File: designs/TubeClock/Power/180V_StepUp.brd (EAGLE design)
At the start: 52 x 39 mm, 16 parts, among them IC1 MAX1771, Q1 RF644

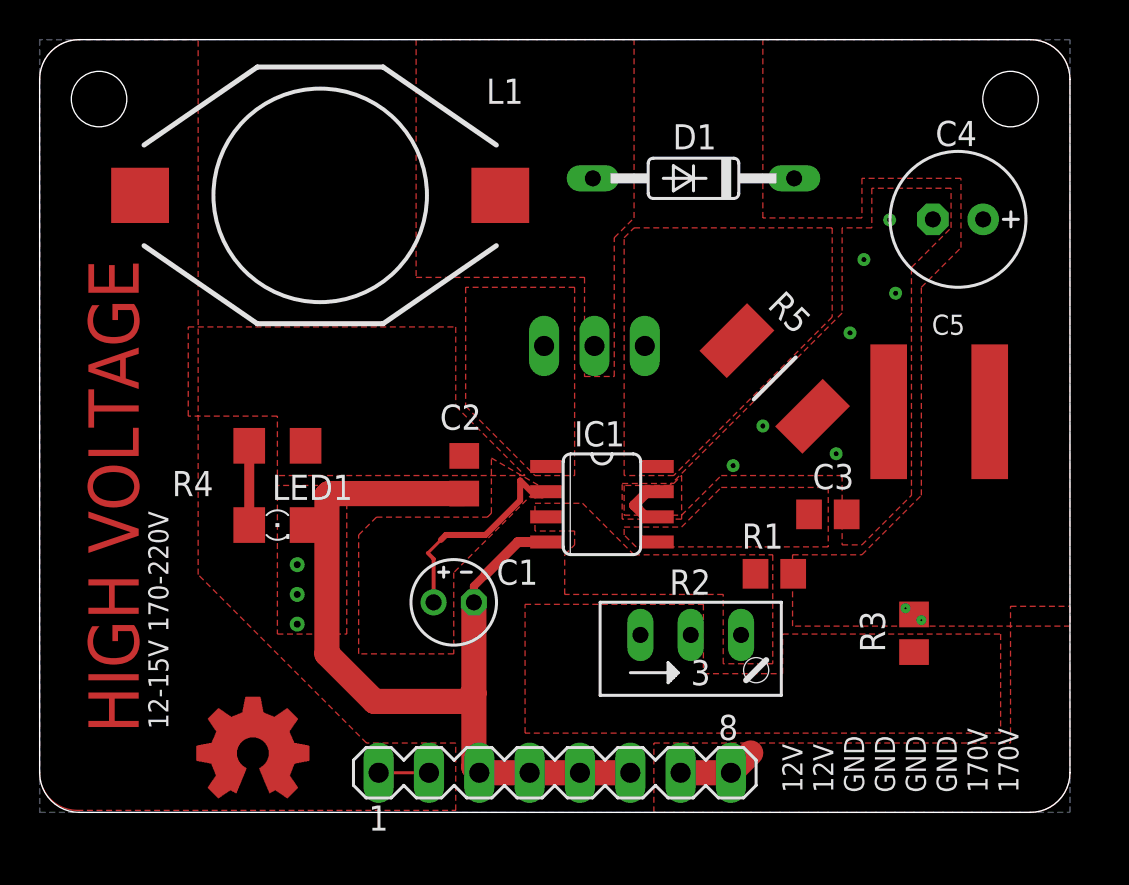
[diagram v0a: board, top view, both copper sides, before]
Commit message: small changes to easter radio mainboard started for in14 nixi tubes and cleanup
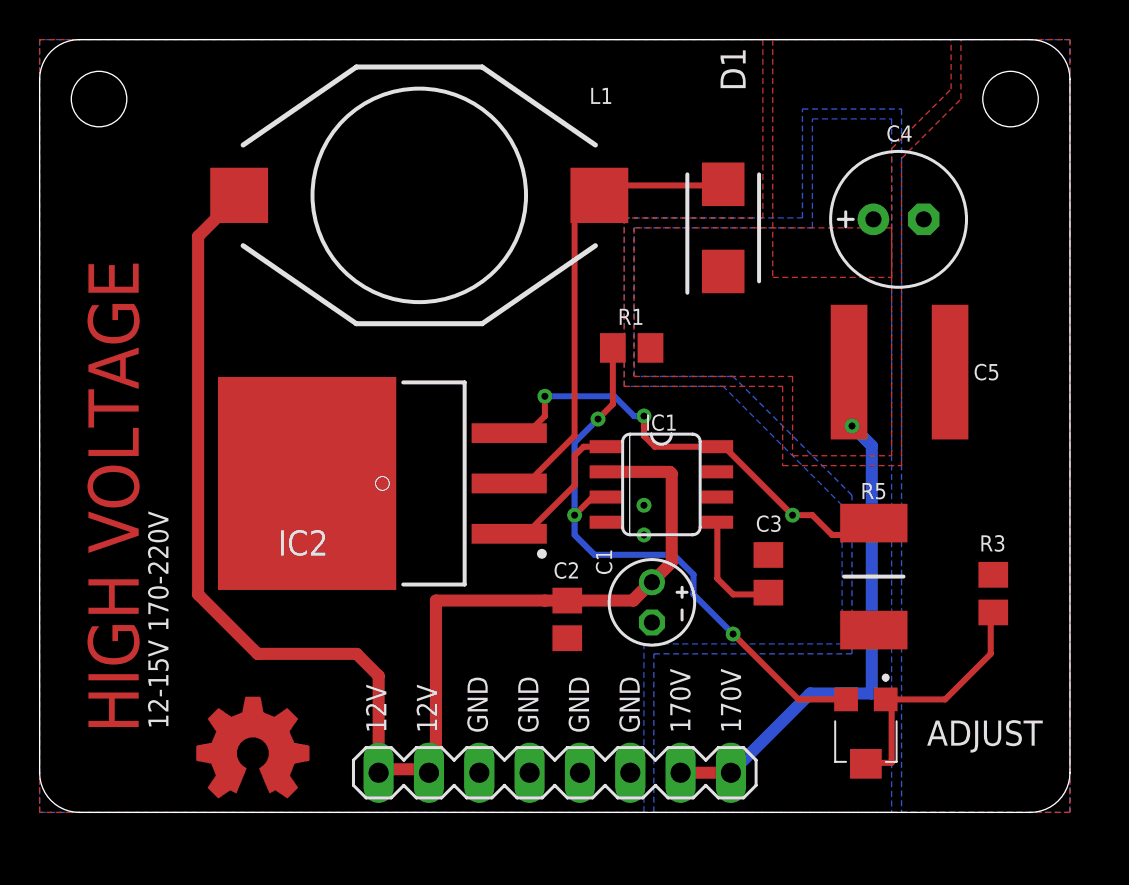
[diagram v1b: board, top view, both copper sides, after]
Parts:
- removed LED1: GREEN, CommonParts:1206
- removed Q1: RF644, transistor-power:TO220BV
- removed R2: 10k, pot:RJ9W
- removed R4: 1K, CommonParts:R1206
- removed SV2: (no value), con-lstb:MA08-1
- added ADJUST: EVM3YSX50B14, CommonParts:EVM3YSX50B14
- added IC2: IRF644SPBF, MouserUseful:TO254P1524X483-4N
- added SV1: (no value), CommonParts:MA08-1
- D1: value 1N4148DO35-10 -> LSM115JE3_TR13; device diode:DO35-10 -> CommonParts:DIOM5436X330N
- moved R1 13.5 mm to (28.9, 23.4)
- moved R5 11.2 mm to (41.1, 11.9), turned to 90 degrees
- moved C1 10.0 mm to (29.9, 10.6), turned to 270 degrees
- moved C2 8.96 mm to (25.6, 9.74)
- moved L1 5.00 mm to (18.2, 31.1)
- moved R3 4.47 mm to (47.1, 11.0)
- moved C3 4.24 mm to (35.8, 12.0), turned to 90 degrees
- moved IC1 3.16 mm to (30.4, 16.6)
- moved C4 3.00 mm to (42.4, 29.9), turned to 0 degrees
- moved D1 2.92 mm to (33.5, 29.5), turned to 90 degrees
- moved C5 2.83 mm to (42.4, 22.2), turned to 0 degrees
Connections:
- removed net N$1: LED1.A, R4.2
- net +170V: now also D1.1, SV1.7, SV1.8; no longer D1.C, SV2.7, SV2.8
- net GND: now also SV1.3, SV1.4, SV1.5, SV1.6; no longer LED1.C, SV2.3, SV2.4, SV2.5, SV2.6
- net N$2: now also D1.2, IC2.2; no longer D1.A, Q1.D
- net N$4: now also IC2.1; no longer Q1.G
- net N$5: now also IC2.3; no longer Q1.S
- net N$6: now also ADJUST.C1; no longer R2.A
- net N$7: now also ADJUST.A1, ADJUST.B1; no longer R2.E, R2.S
- net VIN: now also SV1.1, SV1.2; no longer R4.1, SV2.1, SV2.2
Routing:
- net VIN: track 14.4 -> 75.0 mm
- net GND: track 48.8 -> 0.00 mm, vias 12 -> 2
- net N$6: track 0.00 -> 29.9 mm, vias 0 -> 3
- net N$2: track 0.00 -> 23.8 mm
- net N$5: track 0.00 -> 23.8 mm, vias 0 -> 3
- net +170V: track 3.95 -> 25.2 mm, vias 0 -> 1
- net N$7: track 0.00 -> 12.9 mm
- net N$4: track 0.00 -> 7.56 mm
- net N$3: track 0.00 -> 5.79 mm
- net N$1: track 4.00 -> 0.00 mm
- added copper zone on layer 16, net +170V
- removed copper zone on layer 1, net N$2
- removed copper zone on layer 1, net N$3
- removed copper zone on layer 1, net N$4
- removed copper zone on layer 1, net N$5
- removed copper zone on layer 1, net N$6
- removed copper zone on layer 1, net N$7
- removed copper zone on layer 1, net VIN

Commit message: changed mainboard design radio
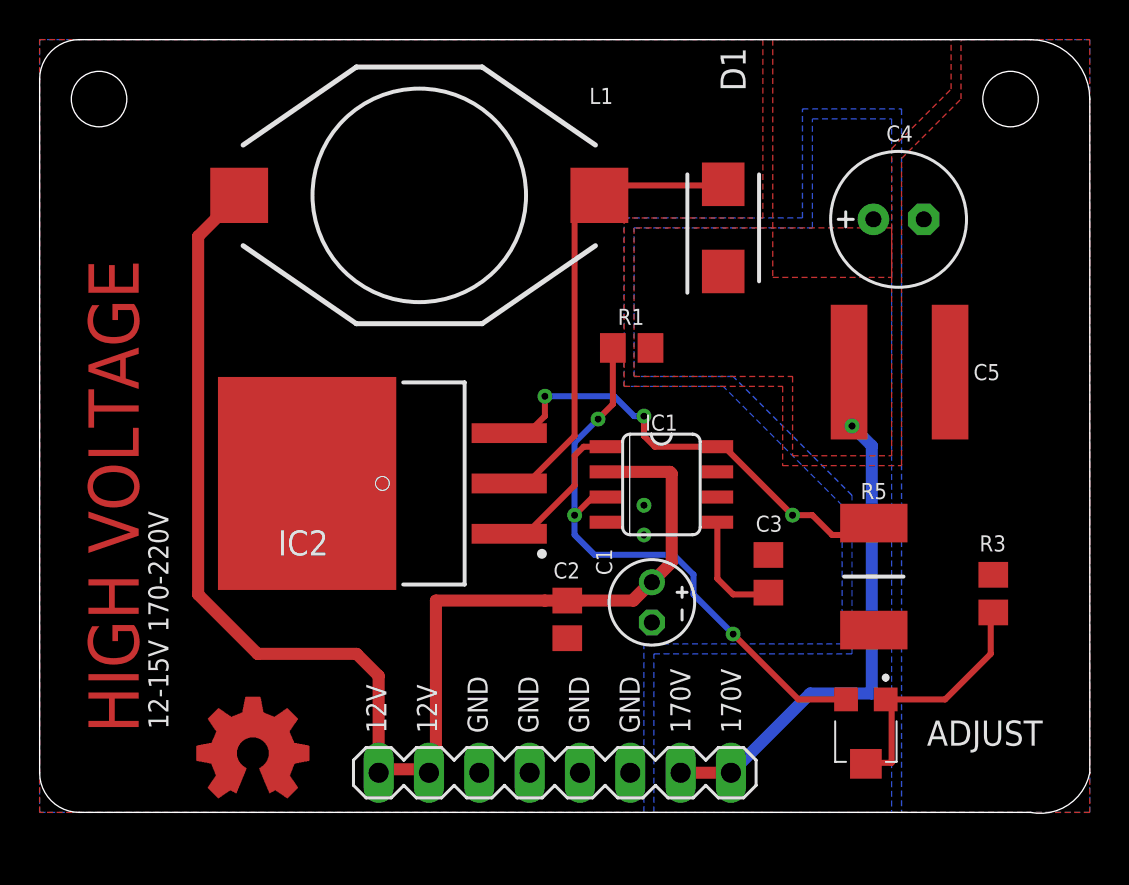
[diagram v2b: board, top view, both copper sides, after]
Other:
- board size 52 x 39 mm -> 53 x 39 mm
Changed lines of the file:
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@@
 <setting verticaltext="up"/>
 </settings>
-<grid distance="0.5" unitdist="mm" unit="mm" style="lines" multiple="1" display="yes" altdistance="5" altunitdist="mil" altunit="mil"/>
+<grid distance="1" unitdist="mm" unit="mm" style="lines" multiple="1" display="yes" altdistance="5" altunitdist="mil" altunit="mil"/>
 <layers>
 <layer number="1" name="Top" color="4" fill="1" visible="yes" active="yes"/>
@@
 </layers>
 <board>
-<fusionsync huburn="a.cGVyc29uYWw6dWUyYTNmMDU1" projecturn="a.cGVyc29uYWw6dWUyYTNmMDU1IzIwMTgxMjEwMTY0OTQ5MjI2" f3durn="urn:adsk.wipprod:dm.lineage:EW_nxjs3TOeM8ciUlo7Bhg" pcbguid="f30d4857-b7eb-4cd6-9f83-62fb7e7f0654" lastpulledtime="" lastsyncedchangeguid="e5bd292d-e348-6bac-0a30-bca2dcfeea96" latestrevisionid="" lastsyncedrevisionid="" lastboardhashguid="" lastpushedtime="" linktopcb3d="false"/>
+<fusionsync huburn="a.cGVyc29uYWw6dWUyYTNmMDU1" projecturn="a.cGVyc29uYWw6dWUyYTNmMDU1IzIwMTgxMjEwMTY0OTQ5MjI2" f3durn="urn:adsk.wipprod:dm.lineage:EW_nxjs3TOeM8ciUlo7Bhg" pcbguid="f30d4857-b7eb-4cd6-9f83-62fb7e7f0654" lastpulledtime="" lastsyncedchangeguid="e5bd292d-e348-6bac-0a30-bca2dcfeea96" latestrevisionid="" lastsyncedrevisionid="" lastboardhashguid="a5e7afaf-2fa9-2cd0-933a-33ae002bcec1" lastpushedtime="2021-02-01T17:02:43Z" linktopcb3d="false"/>
 <plain>
-<wire x1="51" y1="2" x2="51" y2="37" width="0" layer="20"/>
-<wire x1="51" y1="37" x2="49" y2="39" width="0" layer="20" curve="90"/>
+<wire x1="52" y1="2" x2="52" y2="36" width="0" layer="20"/>
+<wire x1="52" y1="36" x2="49" y2="39" width="0" layer="20" curve="90"/>
 <wire x1="49" y1="39" x2="1" y2="39" width="0" layer="20"/>
 <wire x1="1" y1="39" x2="-1" y2="37" width="0" layer="20" curve="90"/>
@@
 <wire x1="-1" y1="2" x2="1" y2="0" width="0" layer="20" curve="90"/>
 <wire x1="1" y1="0" x2="49" y2="0" width="0" layer="20"/>
-<wire x1="49" y1="0" x2="51" y2="2" width="0" layer="20" curve="90"/>
+<wire x1="49" y1="0" x2="52" y2="2" width="0" layer="20" curve="90"/>
 <hole x="2" y="36" drill="2.8"/>
 <hole x="48" y="36" drill="2.8"/>
@@
 <vertex x="45.5" y="36"/>
 <vertex x="45.5" y="39"/>
-<vertex x="51" y="39"/>
-<vertex x="51" y="0"/>
+<vertex x="52" y="39"/>
+<vertex x="52" y="0"/>
 <vertex x="-1" y="0"/>
 <vertex x="-1" y="39"/>
@@
 <vertex x="42.5" y="35.5"/>
 <vertex x="42.5" y="0"/>
-<vertex x="51" y="0"/>
-<vertex x="51" y="39"/>
+<vertex x="52" y="0"/>
+<vertex x="52" y="39"/>
 <vertex x="-1" y="39"/>
 <vertex x="-1" y="0"/>
